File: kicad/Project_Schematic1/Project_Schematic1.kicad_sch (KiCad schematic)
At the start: 42 parts, among them M1 Flag_Servo, M2 Motor1, M3 Motor2, M4 Motor2, Q1 NPN, Q2 NPN, Q3 NPN, U1 74xxx244, U2 PIC32MX170F256B, U3 CD4052, U4 QTR-HD-01A, U5 Drum_LEDs, U6 Timer_LEDs, U7 Intensity_LEDs

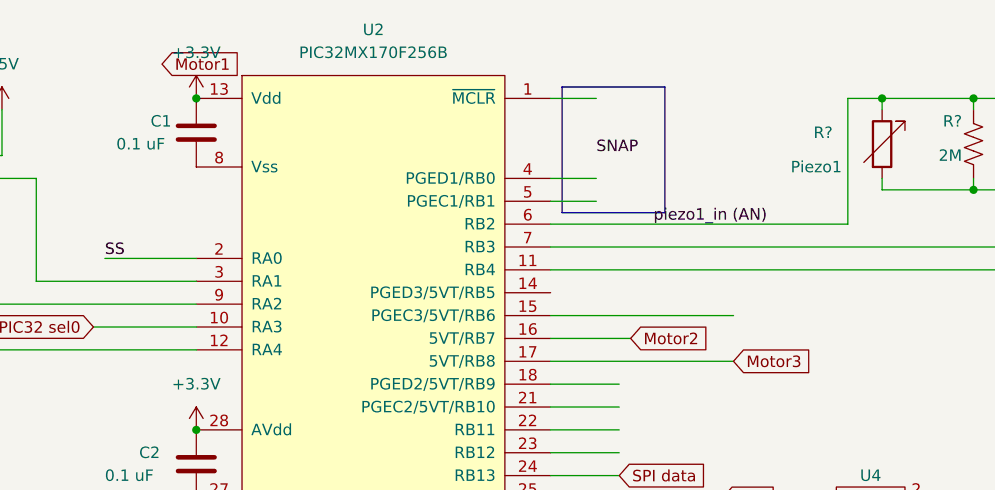
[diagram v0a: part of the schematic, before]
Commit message: Fix kicad label
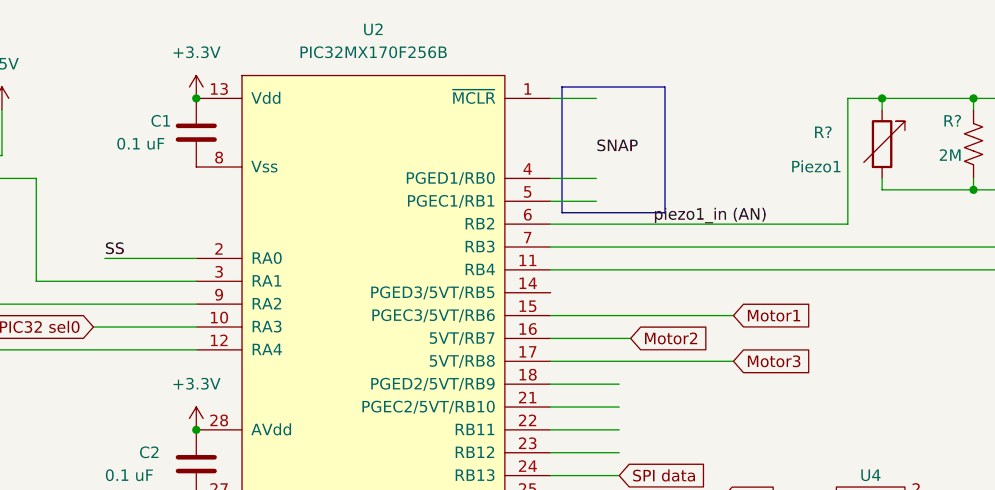
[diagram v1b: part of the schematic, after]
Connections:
- net Motor1: now also U2.15 (PGEC3/5VT/RB6)
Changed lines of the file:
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@@
     )
   )
-  (global_label "Motor1" (shape input) (at 53.34 19.05 0) (fields_autoplaced)
+  (global_label "Motor1" (shape input) (at 116.84 46.99 0) (fields_autoplaced)
     (effects (font (size 1.27 1.27)) (justify left))
-    (property "Intersheet References" "${INTERSHEET_REFS}" (id 0) (at 62.2241 18.9706 0)
+    (property "Intersheet References" "${INTERSHEET_REFS}" (id 0) (at 125.7241 46.9106 0)
       (effects (font (size 1.27 1.27)) (justify left) hide)
     )
